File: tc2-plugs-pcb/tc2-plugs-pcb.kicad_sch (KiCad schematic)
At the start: 51 parts, among them J101 JCON_M12_02Pin, J102 JCON_M16_04Pin, J103 Conn_02x04_Odd_Even, Q101 Q_PMOS_GSD, U101 TPS54331, U102 TPS54331

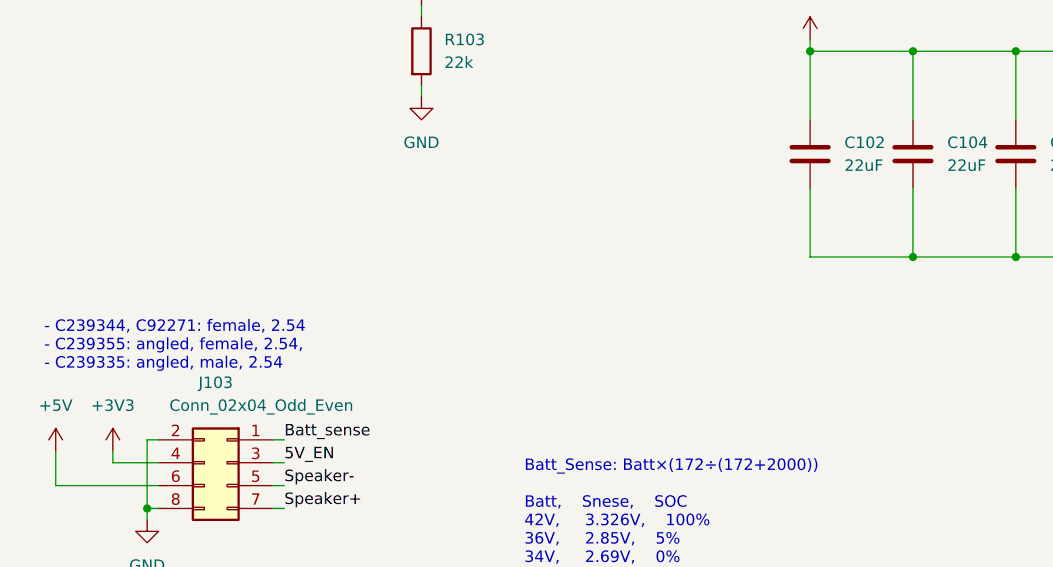
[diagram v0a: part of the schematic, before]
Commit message: Clean up of files and updated drawings for PCBs
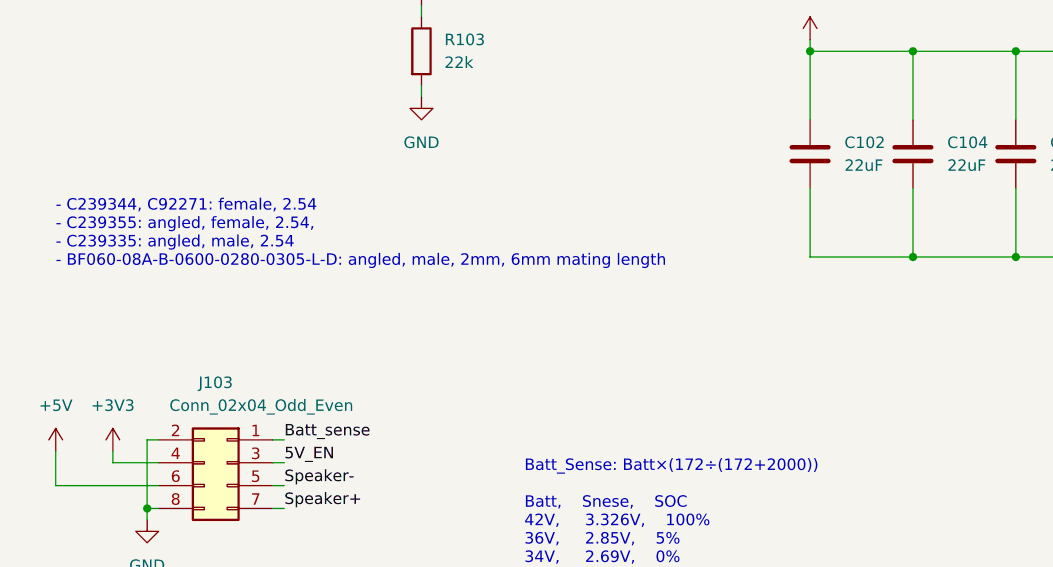
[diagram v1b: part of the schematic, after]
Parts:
- J103: footprint Connector_PinHeader_2.54mm:PinHeader_2x04_P2.54mm_Horizontal -> Connector_PinHeader_2.00mm:PinHeader_2x04_P2.00mm_Horizontal; Digikey (none) -> BF060-08A-B-0600-0280-0305-L-D
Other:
- note added: "- C239344, C92271: female, 2.54 - C239355: angled, female, 2.54, - C239335: angled, male, 2.54 - BF060-08A-B-0600-0280-0305-L-D: angled, male, 2mm, 6mm mating length"
- note removed: "- C239344, C92271: female, 2.54 - C239355: angled, female, 2.54, - C239335: angled, male, 2.54"

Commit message: Version 2 WIP
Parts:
- removed C108: 220uF, Capacitor_SMD:CP_Elec_8x10, symbol Device:C_Polarized
- D101: footprint cacophony-footprints:LL-34_L3.5-W1.5-RD -> cacophony-library:LL-34_L3.5-W1.5-RD
- J101: symbol cacophony-symbols:JCON_M12_02Pin -> cacophony-library:JCON_M12_02Pin
- J102: symbol cacophony-symbols:JCON_M16_04Pin -> cacophony-library:JCON_M16_04Pin
- J103: footprint Connector_PinHeader_2.00mm:PinHeader_2x04_P2.00mm_Horizontal -> cacophony-library:PinHeader_2x04_P2.00mm_Horizontal; LCSC C239355 -> (none)
- L101, L102: footprint cacophony-footprints:IND-SMD_L8.0-W8.0_1217AS -> cacophony-library:IND-SMD_L8.0-W8.0_1217AS
- U101, U102: symbol cacophony-symbols:TPS54331 -> cacophony-library:TPS54331
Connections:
- no-connect marks 1 -> 2
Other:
- note added: "570kHz fixed switching frequency"
- moved on the sheet: C105

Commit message: P2 milestone
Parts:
- removed J101: JCON_M12_02Pin, cacophony-library:jcon-2pin-m12, symbol cacophony-library:JCON_M12_02Pin
- removed J103: Conn_02x04_Odd_Even, cacophony-library:PinHeader_2x04_P2.00mm_Horizontal, symbol Connector_Generic:Conn_02x04_Odd_Even
- added C38, C43: 10uF, Capacitor_SMD:C_0603_1608Metric, symbol Device:C_Small
- added J103: JCON_M16_06Pin, cacophony-library:jcon-6pin-m16, symbol cacophony-library:JCON_M16_06Pin
- added J104: Conn_02x06_Odd_Even, cacophony-library:PinHeader_2x06_P2.00mm_Horizontal, symbol Connector_Generic:Conn_02x06_Odd_Even
- added Q1: Q_PMOS_GSD, Package_TO_SOT_SMD:SOT-23, symbol Device:Q_PMOS_GSD
- added Q3: 2N7002, Package_TO_SOT_SMD:SOT-23, symbol Transistor_FET:2N7002
- added R14: 1k, Resistor_SMD:R_0402_1005Metric, symbol Device:R
- added R38: 100k, Resistor_SMD:R_0402_1005Metric, symbol Device:R
- added TP6: TestPoint_2Pole, cacophony-library:test-point-2p, symbol Connector:TestPoint_2Pole
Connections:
- net +12V: now also C43.1, Q1.2 (S), R38.2
- net +3V3: now also J104.4 (Pin_4)
- net +5V: now also J104.6 (Pin_6)
- net 5V_EN: now also J104.3 (Pin_3)
- net GND: now also C38.2, C43.2, J103.1, J104.2 (Pin_2), J104.8 (Pin_8), Q3.2 (S), TP6.1
- net Batt_sense renamed BATT_SENSE
- net BATT_SENSE: now also J104.1 (Pin_1)
- new net: Q3.1 (G), R14.2
- new net: Q1.1 (G), Q3.3 (D), R38.1
- new net EN_PERIPH: J104.12 (Pin_12), R14.1
- new net OUT_RX: J103.2, J104.11 (Pin_11)
- new net OUT_TX: J103.3, J104.9 (Pin_9)
- new net SPEAKER_+: J103.4, J104.5 (Pin_5)
- new net SPEAKER_-: J103.5, J104.7 (Pin_7)
- new net VOUT: C38.1, J103.6, Q1.3 (D), TP6.2
- no-connect marks 2 -> 3
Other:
- moved on the sheet: J102, R101, R102, R103

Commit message: P3-Nov release
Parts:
- removed J103: JCON_M16_06Pin, cacophony-library:jcon-6pin-m16, symbol cacophony-library:JCON_M16_06Pin
- removed Q3: 2N7002, Package_TO_SOT_SMD:SOT-23, symbol Transistor_FET:2N7002
- added FB1 (x2): FerriteBead, Inductor_SMD:L_0805_2012Metric, symbol Device:FerriteBead
- added J101: JCON_M16_2+4Pin, cacophony-library:jcon-2+4pin-m16, symbol cacophony-library:JCON_M16_2+4Pin
- added Q1: AO3400A, Package_TO_SOT_SMD:SOT-23, symbol Transistor_FET:AO3400A
- added R115: 2M, Resistor_SMD:R_1210_3225Metric, symbol Device:R
- added R116: 560k, Resistor_SMD:R_1206_3216Metric, symbol Device:R
- added R117: 33k, Resistor_SMD:R_0603_1608Metric, symbol Device:R
- added R38: 100k, Resistor_SMD:R_0402_1005Metric, symbol Device:R
- added TP6 (x2): TestPoint_2Pole, cacophony-library:test-point-2p, symbol Connector:TestPoint_2Pole
- C121, C122, C123, C124, C125, C126, C127, C128: LCSC C86295 -> C2980159
- R102: LCSC C74850 -> C136927
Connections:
- net +3V3: now also J104.10 (Pin_10), FB1.2, TP6.2; no longer C120.1, C122.1, C124.1, C126.1, C128.1, J104.4 (Pin_4), L102.2, R112.1
- net +5V: now also J104.8 (Pin_8), FB1.2, TP6.2; no longer C119.1, C121.1, C123.1, C125.1, C127.1, J104.6 (Pin_6), L101.2, R110.1
- net +Batt: now also R115.1
- net 5V_EN: now also J104.1 (Pin_1); no longer J104.3 (Pin_3)
- net GND: now also J104.12 (Pin_12), J104.6 (Pin_6), J101.1, Q1.2 (S), R117.2, R38.1, TP6.1, TP6.1; no longer J104.2 (Pin_2), J104.8 (Pin_8)
- net OUT_RX: now also J104.2 (Pin_2), J101.2; no longer J104.11 (Pin_11)
- net OUT_TX: now also J104.4 (Pin_4), J101.3; no longer J104.9 (Pin_9)
- net SPEAKER_+: now also J104.9 (Pin_9), J101.4; no longer J104.5 (Pin_5)
- net SPEAKER_-: now also J101.5
- net VOUT: now also J101.6
- net at R14.2: now also Q1.1 (G), R38.2
- net at Q1.1 (G), R38.1: now also Q1.3 (D)
- net BATT_SENSE renamed BATT_SENSE_HV
- net BATT_SENSE_HV: now also J104.3 (Pin_3); no longer J104.1 (Pin_1)
- net EN_PERIPH renamed EN_PERIPH_POWER
- net EN_PERIPH_POWER: now also J104.11 (Pin_11); no longer J104.12 (Pin_12)
- new net: R116.2, R117.1
- new net 3V3_PF: C120.1, C122.1, C124.1, C126.1, C128.1, FB1.1, L102.2, R112.1
- new net 5V0_PF: C119.1, C121.1, C123.1, C125.1, C127.1, FB1.1, L101.2, R110.1
- new net BATT_SENSE_LV: J104.5 (Pin_5), R115.2, R116.1
- no-connect marks 3 -> 2
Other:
- note added: "Always double check allignemnt with main PCB"
- note removed: "TODO: - Check the pinout of plugs - Check size of pins on plugs - Change Capacitors to something that has smaller leakage current. - C178503"
- moved on the sheet: C38, C43, J102, J104, Q1, R101, R102, R103, R14, R38, TP6
